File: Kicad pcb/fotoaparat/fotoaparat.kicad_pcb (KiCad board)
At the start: 2 copper layers, 104 x 114.5 mm, 36 parts, among them J1 Conn_02x01, J2 Conn_01x02_Socket, Q1 BC547, Q2 BC547, Q3 BC547, Q4 BC547, SW1 SW_Push_Dual, U1 TP4056, U10 VBsemi SI2312CDS-T1-GE3, U11 VBsemi SI2312CDS-T1-GE3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

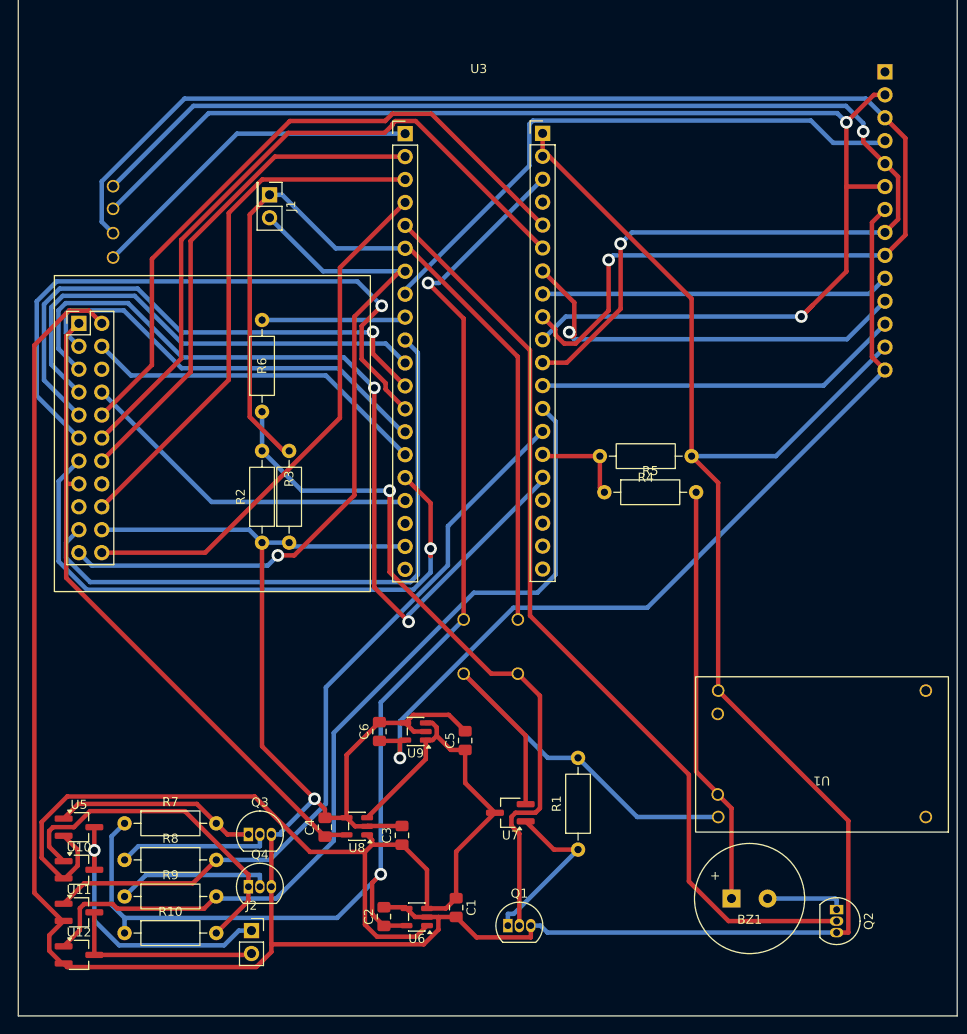
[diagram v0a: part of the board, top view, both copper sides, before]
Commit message: Úprava schémata
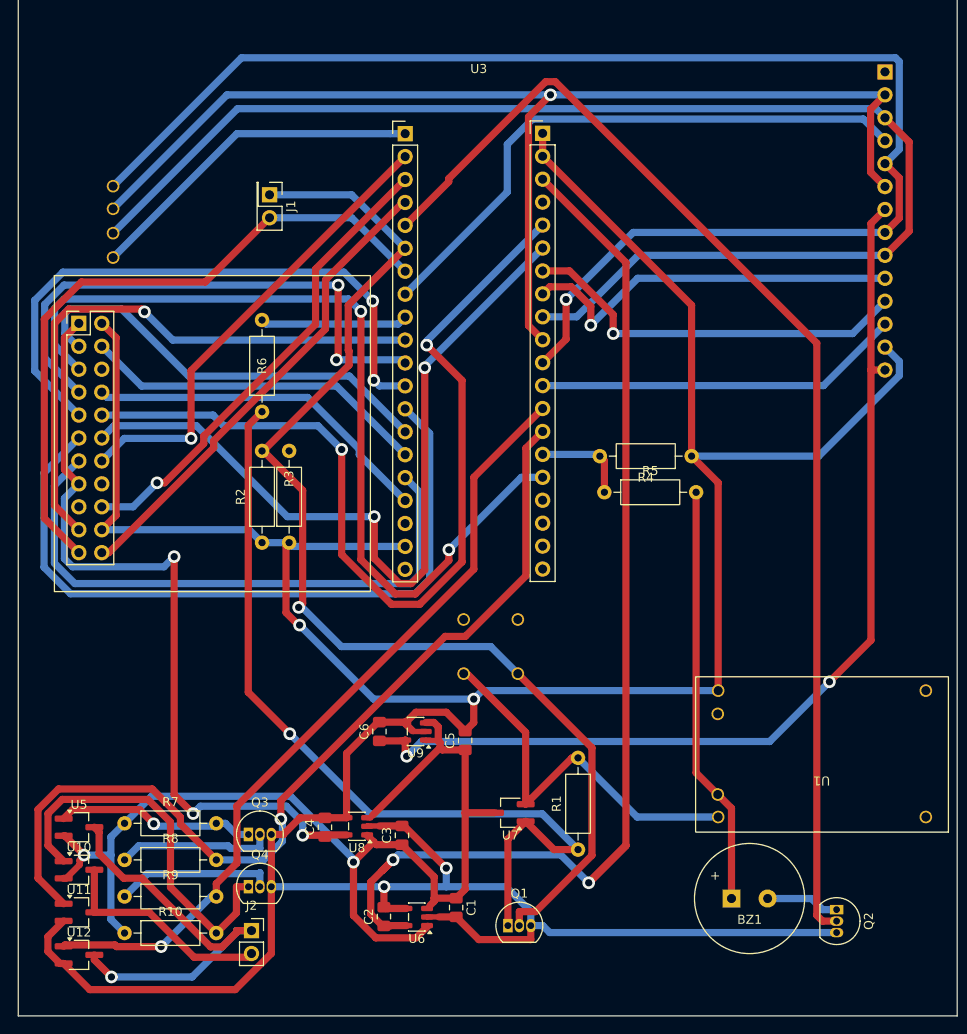
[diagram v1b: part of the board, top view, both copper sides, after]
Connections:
- net Net-(Q2-B) renamed /zvuk
- net Net-(U1-OUT+) renamed /out+
- net Net-(U11-Gate) renamed /dc+
- net Net-(U12-Gate) renamed /dc-
- net Net-(U2-d0) renamed /d0
- net Net-(U2-d1) renamed /d1
- net Net-(U2-d2) renamed /d2
- net Net-(U2-d3) renamed /d3
- net Net-(U2-d4) renamed /d4
- net Net-(U2-d5) renamed /d5
- net Net-(U2-d6) renamed /d6
- net Net-(U2-d7) renamed /d7
- net Net-(U2-rck) renamed /rck
- net Net-(U2-rrst) renamed /rrst
- net Net-(U2-sioc) renamed /sioc
- net Net-(U2-siod) renamed /siod
- net Net-(U2-vsync) renamed /vsync
- net Net-(U3-pa1) renamed /battery
- net Net-(U3-pa11) renamed /t cs
- net Net-(U3-pa4) renamed /lcd cs
- net Net-(U3-pa5) renamed /clk
- net Net-(U3-pa6) renamed /miso
- net Net-(U3-pa7) renamed /mosi
- net Net-(U3-pb0) renamed /dc
- net Net-(U3-pb1) renamed /reset
- net Net-(U3-pb12) renamed /sd cs
- J1 pad 1: /tx -> /tx + pow hold
- Q1 pad 1: Net-(Q1-C) -> pow hold
- Q1 pad 2: Net-(Q1-B) -> /tx + pow hold
- R1 pad 1: Net-(Q1-C) -> pow hold
- R10 pad 1: +3.3V -> +4V
- R2 pad 2: Net-(Q1-B) -> /tx + pow hold
- R6 pad 1: Net-(Q1-B) -> pow hold
- R7 pad 1: +3.3V -> +4V
- SW1 pad 1: /tx -> unconnected-(SW1-Pad1)
- SW1 pad 2: +3.3V -> unconnected-(SW1-Pad2)
- SW1 pad 3: Net-(Q1-B) -> /tx + pow hold
- U10 pad 3: Net-(J2-Pin_1) -> Net-(J2-Pin_2)
- U12 pad 3: Net-(J2-Pin_2) -> Net-(J2-Pin_1)
- U3 pad 6: /tx -> /tx + pow hold
- U7 pad 1: Net-(Q1-C) -> pow hold
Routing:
- net /tx + pow hold: track 0.00 -> 129.0 mm, vias 0 -> 1
- net /tx: track 95.5 -> 0.00 mm
- net pow hold: track 0.00 -> 94.9 mm, vias 0 -> 1
- net Net-(Q1-B): track 80.1 -> 0.00 mm, vias 1 -> 0
- net GND: track 430.9 -> 401.6 mm, vias 1 -> 4
- net /d4: track 74.6 -> 101.6 mm, vias 0 -> 2
- net /zvuk: track 103.9 -> 130.2 mm
- net /miso: track 156.0 -> 131.0 mm, vias 2 -> 1
- net Net-(Q1-C): track 19.1 -> 0.00 mm
- net /dc+: track 84.8 -> 103.0 mm, vias 0 -> 1
- net +3.3V ov7670: track 73.2 -> 90.0 mm, vias 0 -> 3
- net Net-(J2-Pin_1): track 31.7 -> 46.2 mm
- net +3.3V lcd: track 97.7 -> 111.4 mm, vias 1 -> 2
- net /mosi: track 161.6 -> 149.8 mm, vias 1 -> 0
- net /dc-: track 99.6 -> 88.4 mm, vias 0 -> 1
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
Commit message: Gnd plane
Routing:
- added copper zone on B.Cu, net GND
- added copper zone on F.Cu, net GND
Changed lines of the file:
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@@
 		(net 61)
+	)
+	(zone
+		(net 6)
+		(net_name "GND")
+		(layers "F.Cu" "B.Cu")
+		(hatch edge 0.5)
+		(connect_pads
+			(clearance 0.3)
+		)
+		(min_thickness 0.25)
+		(filled_areas_thickness no)
+		(fill yes
+			(thermal_gap 0.5)
+			(thermal_bridge_width 0.5)
+		)
+		(polygon
+			(pts
+				(xy 95 38.5) (xy 91.5 38) (xy 91.5 156.5) (xy 206 157) (xy 209.5 38)
+			)
+		)
 	)
 	(embedded_fonts no)

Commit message: Resistory
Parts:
- added R11: 1k, Resistor_THT:R_Axial_DIN0207_L6.3mm_D2.5mm_P10.16mm_Horizontal, F.Cu at (184.9, 139.0)
- added R12: 1k, Resistor_THT:R_Axial_DIN0207_L6.3mm_D2.5mm_P10.16mm_Horizontal, F.Cu at (156.0, 132.6)
- R2: value 100k -> 50k
- R3: value 10k -> 100
- R6: value 50k -> 1k
- moved U6 85.7 mm to (163.5, 61.5)
- moved C2 85.6 mm to (159.5, 61.5)
- moved C1 83.5 mm to (167.0, 62.5), turned to 90 degrees
- moved C6 66.3 mm to (189.4, 82.5)
- moved U9 59.5 mm to (187.9, 86.5), turned to 0 degrees
- moved R3 59.3 mm to (171.9, 142.5), turned to 0 degrees
- moved R6 55.4 mm to (147.0, 139.2)
- moved C5 52.8 mm to (184.4, 87.5)
- moved R2 49.0 mm to (148.0, 59.9), turned to -90 degrees
- moved C3 36.8 mm to (109.5, 115.0)
- moved U8 35.7 mm to (105.9, 114.0)
- moved C4 35.7 mm to (101.7, 115.1), turned to 180 degrees
- moved R9 28.6 mm to (134.5, 128.5), turned to -90 degrees
- moved BZ1 27.8 mm to (156.8, 134.0), turned to -90 degrees
- moved R10 26.9 mm to (115.4, 120.0)
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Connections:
- net Net-(U2-wr) renamed /wr
- Q1 pad 1: pow hold -> /pow hold
- Q1 pad 2: /tx + pow hold -> Net-(Q1-B)
- Q2 pad 1: Net-(BZ1--) -> Net-(Q2-C)
- Q2 pad 2: /zvuk -> Net-(Q2-B)
- R1 pad 1: pow hold -> /pow hold
- R3 pad 1: GND -> Net-(BZ1--)
- R3 pad 2: /tx -> Net-(Q2-C)
- R6 pad 1: pow hold -> /pow hold
- R6 pad 2: Net-(U3-pa12) -> /pow hold
- U3 pad 9: Net-(U3-pa12) -> /pow hold
- U6 pad 4: GND -> unconnected-(U6-NC-Pad4)
- U7 pad 1: pow hold -> /pow hold
- U8 pad 4: GND -> unconnected-(U8-NC-Pad4)
- U9 pad 4: GND -> unconnected-(U9-NC-Pad4)
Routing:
- net GND: track 401.6 -> 0.00 mm, vias 4 -> 0
- net +3.3V: track 148.3 -> 6.73 mm, vias 2 -> 0
- net +4V: track 127.4 -> 248.2 mm, vias 2 -> 0
- net /pow hold: track 0.00 -> 100.1 mm
- net pow hold: track 94.9 -> 0.00 mm, vias 1 -> 0
- net +3.3V lcd: track 111.4 -> 24.5 mm, vias 2 -> 0
- net +3.3V ov7670: track 90.0 -> 41.4 mm, vias 3 -> 1
- net /tx + pow hold: track 129.0 -> 80.7 mm, vias 1 -> 0
- net /zvuk: track 130.2 -> 94.1 mm
- net /mosi: track 149.8 -> 183.0 mm, vias 0 -> 1
- net /clk: track 160.5 -> 128.2 mm, vias 1 -> 0
- net /d5: track 67.4 -> 98.2 mm, vias 2 -> 3
- net +BATT: track 46.6 -> 17.5 mm
- net Net-(J2-Pin_1): track 46.2 -> 17.9 mm
- net /d4: track 101.6 -> 73.4 mm, vias 2 -> 0
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
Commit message: Úprava schéma
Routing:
- net /vsync: track 122.1 -> 96.2 mm, vias 5 -> 2
- net +3.3V ov7670: track 41.4 -> 60.9 mm, vias 1 -> 0
- net /miso: track 144.4 -> 163.2 mm, vias 1 -> 2
- net /clk: track 128.2 -> 145.6 mm, vias 0 -> 1
- net /d2: track 89.0 -> 73.5 mm, vias 1 -> 0
- net /pow hold: track 100.1 -> 86.9 mm
- net /zvuk: track 94.1 -> 107.1 mm, vias 0 -> 1
- net /dc+: track 98.4 -> 87.8 mm, vias 1 -> 0
- net /d5: track 98.2 -> 91.2 mm, vias 3 -> 0
- net /t cs: track 76.4 -> 69.6 mm, vias 3 -> 0
- net /out+: track 66.6 -> 59.9 mm
- net /d3: track 75.1 -> 81.5 mm, vias 2 -> 0
- net /wr: track 71.8 -> 65.4 mm
- net /mosi: track 183.0 -> 176.8 mm
- net /reset: track 39.3 -> 44.7 mm
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
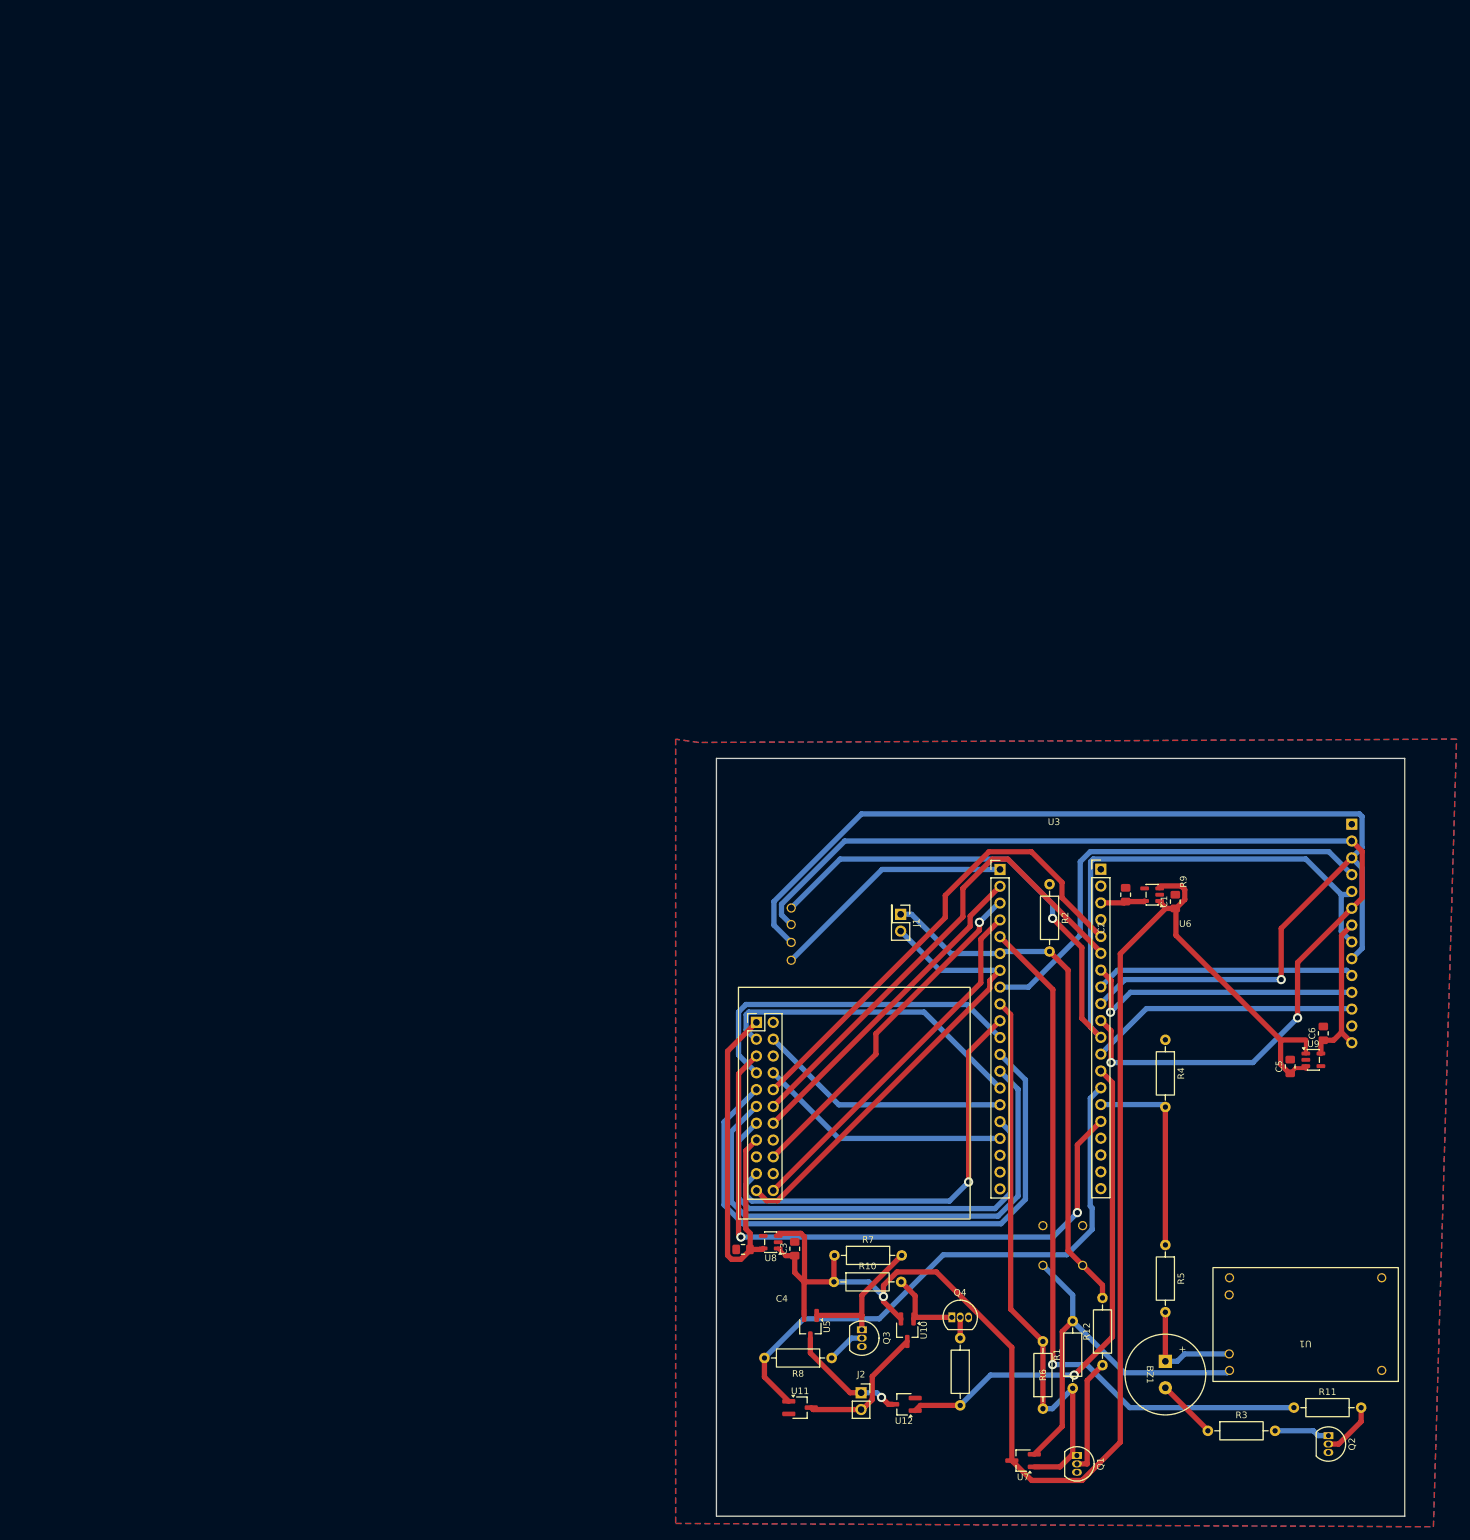
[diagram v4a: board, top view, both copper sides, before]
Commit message: Menší deska a větší plošky pro pájení
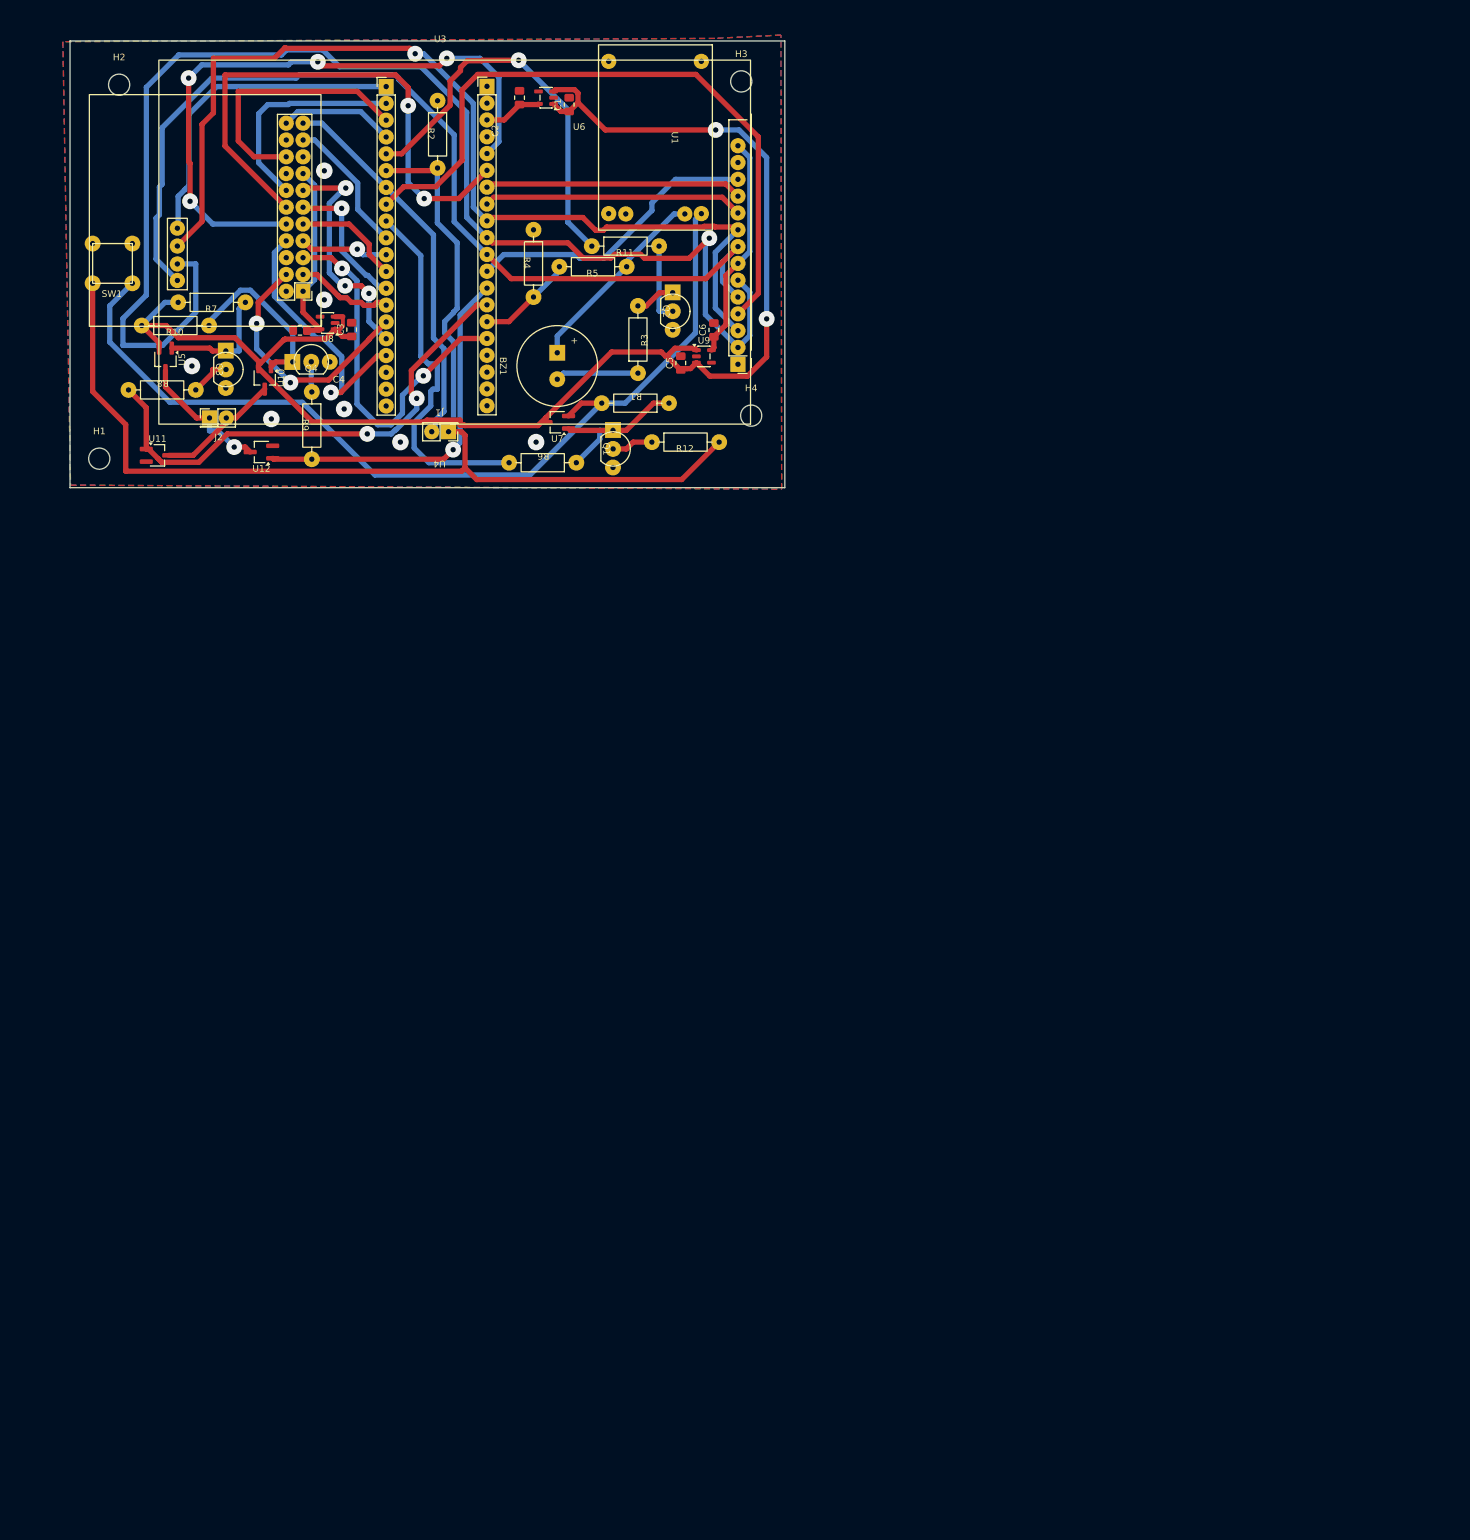
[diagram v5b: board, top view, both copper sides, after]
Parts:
- added H1: MountingHole, MountingHole:MountingHole_3.2mm_M3, F.Cu at (4.42, -4.38)
- added H2: MountingHole, MountingHole:MountingHole_3.2mm_M3, F.Cu at (7.42, -60.9)
- added H3: MountingHole, MountingHole:MountingHole_3.2mm_M3, F.Cu at (101.4, -61.4)
- added H4: MountingHole, MountingHole:MountingHole_3.2mm_M3, F.Cu at (102.9, -10.9)
- J1: footprint Connector_PinHeader_2.54mm:PinHeader_2x01_P2.54mm_Vertical -> txrx:txrx
- J2: footprint Connector_PinSocket_2.54mm:PinSocket_1x02_P2.54mm_Vertical -> txrx:txrx
- Q1, Q2, Q3, Q4: footprint Package_TO_SOT_THT:TO-92_Inline -> transistor:npnTHT
- R1, R10, R11, R12, R2, R3, R4, R5, R6, R7, R8, R9: footprint Resistor_THT:R_Axial_DIN0207_L6.3mm_D2.5mm_P10.16mm_Horizontal -> resistorTHT:thtRESISTOR
- SW1, U4: moved to F.Cu
- moved U1 220.8 mm to (79.9, -66.9), turned to -90 degrees
- moved SW1 210.8 mm to (3.32, -30.9), turned to 0 degrees
- moved R11 201.2 mm to (83.8, -35.0)
- moved Q2 197.4 mm to (89.6, -26.7)
- moved U4 186.2 mm to (102.8, -64.6)
- moved R3 185.2 mm to (87.3, -22.3), turned to 90 degrees
- moved R8 179.0 mm to (14.0, -16.3)
- moved BZ1 177.9 mm to (64.9, -18.4)
- moved U2 177.1 mm to (36.9, -56.8), turned to 180 degrees
- moved U5 175.7 mm to (14.4, -19.4)
- moved Q3 174.9 mm to (22.0, -17.9)
- moved R10 174.3 mm to (15.8, -23.0)
- moved J2 173.6 mm to (22.4, -7.13)
- moved U10 173.6 mm to (29.4, -16.6)
- moved U11 173.6 mm to (13.2, -4.88)
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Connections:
- R6 pad 2: /pow hold -> /pow hold mcu
- U3 pad 9: /pow hold -> /pow hold mcu
- U6 pad 4: unconnected-(U6-NC-Pad4) -> GND
- U8 pad 4: unconnected-(U8-NC-Pad4) -> GND
- U9 pad 4: unconnected-(U9-NC-Pad4) -> GND
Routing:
- net /tx + pow hold: track 80.7 -> 181.7 mm
- net /out+: track 59.9 -> 141.1 mm
- net /d5: track 91.2 -> 16.4 mm
- net /pow hold: track 86.9 -> 25.4 mm
- net /d3: track 81.5 -> 21.4 mm, vias 0 -> 1
- net /pow hold mcu: track 0.00 -> 55.4 mm
- net /zvuk: track 107.1 -> 61.0 mm
- net /wr: track 65.4 -> 21.0 mm, vias 1 -> 0
- net /miso: track 163.2 -> 205.6 mm, vias 2 -> 1
- net /vsync: track 96.2 -> 56.2 mm
- net /d7: track 52.4 -> 13.4 mm, vias 0 -> 1
- net /rrst: track 55.1 -> 17.4 mm
- net /t cs: track 69.6 -> 102.5 mm
- net /sioc: track 47.7 -> 14.9 mm
- net +3.3V ov7670: track 60.9 -> 28.1 mm
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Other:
- board size 104 x 114.5 mm -> 108 x 67.5 mm
